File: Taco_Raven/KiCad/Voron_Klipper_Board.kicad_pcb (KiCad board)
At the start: 4 copper layers, 120 x 113 mm, 360 parts, among them J1 CONN_02X05, J10 CONN_01X04, J11 CONN_01X04, J12 CONN_02X03, J13 CONN_01X02, J14 CONN_01X02, J15 CONN_01X02, J16 CONN_01X02, J17 CONN_01X02, J18 CONN_01X02, J19 CONN_01X02, J2 CONN_02X05, J20 CONN_01X02, J21 CONN_01X02, J22 CONN_01X02, J23 CONN_01X02, J24 CONN_01X02, J25 CONN_01X06, J26 CONN_01X02, J27 CONN_01X02, J28 CONN_01X02, J29 CONN_01X03, J3 CONN_01X04, J30 CONN_01X03, J31 CONN_01X03, J32 CONN_01X03, J33 CONN_01X03, J34 USB_MINI, J35 CONN_02X05, J36 CONN_02X04, J4 CONN_01X04, J5 CONN_01X04, J6 CONN_01X04, J7 CONN_01X04, J8 CONN_01X04, J9 CONN_01X04, SW1 SW_Push, U1 TMC2130, U10 PMV40UN, U11 PMV40UN, U12 PMV40UN, U13 PMV40UN, U14 CSD18532, U15 CSD18532, U16 CSD18532, U17 CSD18532, U18 AP2112-3.3, U19 A4403, U2 TMC2130, U20 A4403, U21 ATSAMD51, U22 SPIFLASH_SOIC8, U23 PMV40UN, U3 TMC2130, U4 TMC2130, U5 TMC2130, U6 TMC2130, U7 TMC2130, U8 TMC2130, U9 PMV40UN

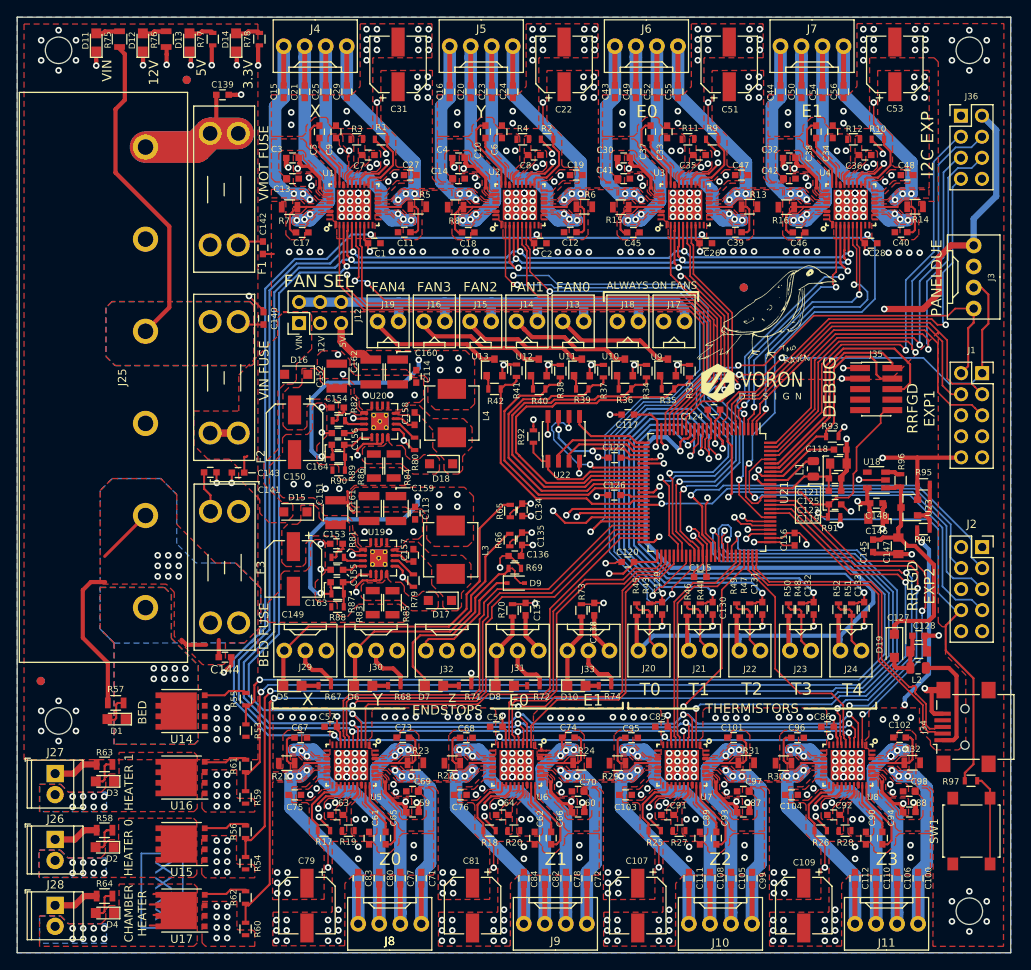
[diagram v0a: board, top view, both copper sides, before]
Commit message: Update Schematic and PCB with RevB changes
Changelog:
Footprints for J1, J2 have been mirrored.
4.7K pullups for EXP_I2C_SDA,SCL have been added.
Current sense resistors for the TMC drivers have ben lowered from 0.22Ohm to 0.11ohm to allow for more current.
Fan headers have been mirrored from Duet.
Thermistor circuits have been fixed.
R81 changed to 200k.
C163, C164 Feedforward capacitors reduced to 8.2nF and 10nF respectively.
R89 dropped to 3.48k,
R83,R84, R85,R86 Current sense kelvin connection has been improved.
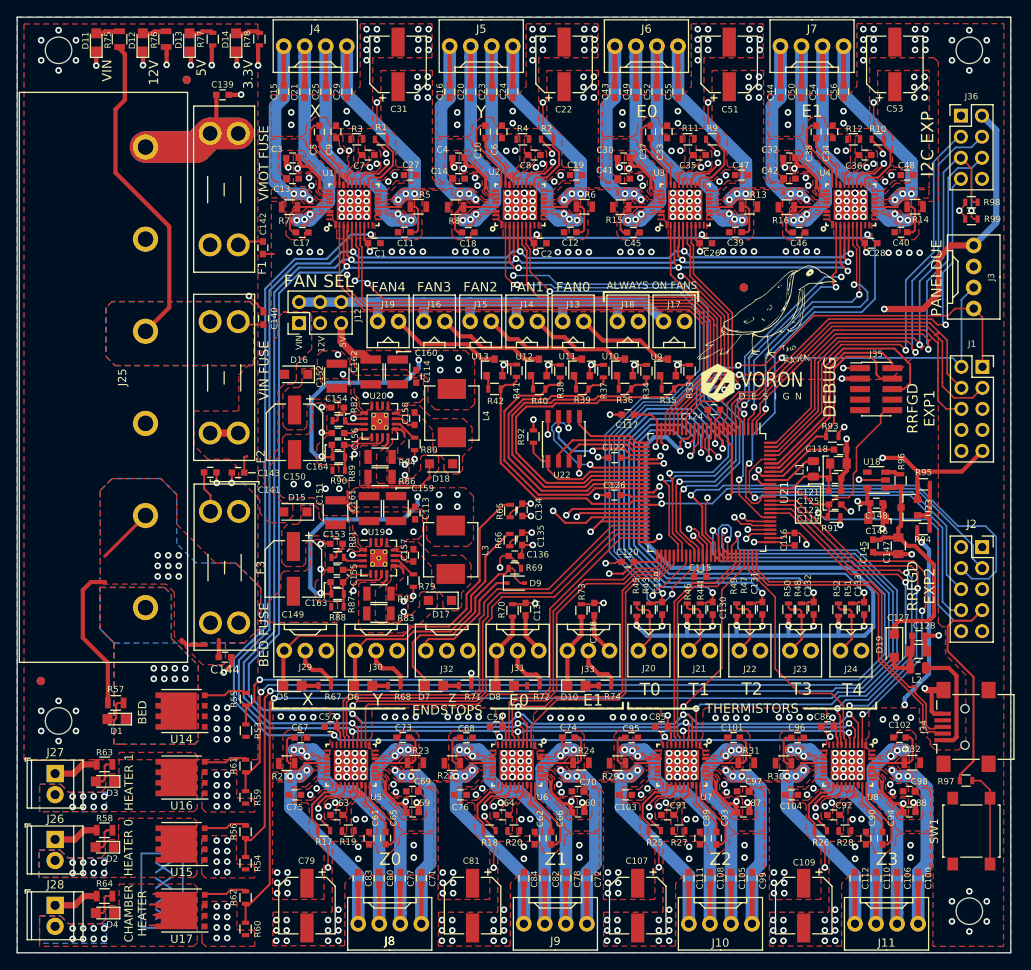
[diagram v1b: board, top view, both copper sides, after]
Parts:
- added R98: 4.70K, MZBOT:R_0603, F.Cu at (225.3, 62.4)
- added R99: 4.70K, MZBOT:R_0603, F.Cu at (225.3, 64.4)
- C163: value 100nF -> 8.2nF
- C164: value 100nF -> 10nF
- R13, R14, R15, R16, R21, R22, R23, R24, R29, R30, R31, R32, R5, R6, R7, R8: value 0R22 -> 0R11
- R43, R44, R47, R48, R51: value 10.0K -> 1.00K
- R81: value 100K -> 200K
- R89: value 3.60K -> 3.48K
- moved R85 1.97 mm to (153.7, 109.6), turned to 0 degrees
- moved R84 1.97 mm to (153.8, 93.1), turned to 0 degrees
- moved R83 1.50 mm to (153.7, 112.0), turned to 0 degrees
- moved R86 1.49 mm to (153.8, 95.5), turned to 0 degrees
- moved J1 0.77 mm to (226.6, 82.2)
- moved R97 0.60 mm to (224.6, 132.2)
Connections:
- J1 pad 1: PD_RX_RRFGD_BUZ -> PD_TX_RRFGD_BTN_ENC
- J1 pad 10: +5V -> GND
- J1 pad 2: PD_TX_RRFGD_BTN_ENC -> PD_RX_RRFGD_BUZ
- J1 pad 3: RRFGD_LCDE -> RRFGD_LCDRS
- J1 pad 4: RRFGD_LCDRS -> RRFGD_LCDE
- J1 pad 5: RRFGD_LCD4 -> (no net)
- J1 pad 6: (no net) -> RRFGD_LCD4
- J1 pad 9: GND -> +5V
- J13 pad 1: +V_FAN -> Net-(J13-Pad1)
- J13 pad 2: Net-(J13-Pad2) -> +V_FAN
- J14 pad 1: +V_FAN -> Net-(J14-Pad1)
- J14 pad 2: Net-(J14-Pad2) -> +V_FAN
- J15 pad 1: +V_FAN -> Net-(J15-Pad1)
- J15 pad 2: Net-(J15-Pad2) -> +V_FAN
- J16 pad 1: +V_FAN -> Net-(J16-Pad1)
- J16 pad 2: Net-(J16-Pad2) -> +V_FAN
- J17 pad 1: +V_FAN -> GND
- J17 pad 2: GND -> +V_FAN
- J18 pad 1: +V_FAN -> GND
- J18 pad 2: GND -> +V_FAN
- J19 pad 1: +V_FAN -> Net-(J19-Pad1)
- J19 pad 2: Net-(J19-Pad2) -> +V_FAN
- J2 pad 1: SPI_SDI -> SPI_CLK
- J2 pad 10: (no net) -> GND
- J2 pad 2: SPI_CLK -> SPI_SDI
- J2 pad 3: RRFGD_BTN_EN1 -> RRFGD_SDCSEL
- J2 pad 4: RRFGD_SDCSEL -> RRFGD_BTN_EN1
- J2 pad 5: RRFGD_BTN_EN2 -> SPI_SDO
- J2 pad 6: SPI_SDO -> RRFGD_BTN_EN2
- J2 pad 7: RRFGD_SDDET -> RESETN
- J2 pad 8: RESETN -> RRFGD_SDDET
- J2 pad 9: GND -> (no net)
- J20 pad 1: VREF -> Net-(J20-Pad1)
- J20 pad 2: Net-(J20-Pad2) -> GND
- J21 pad 1: VREF -> Net-(J21-Pad1)
- J21 pad 2: Net-(J21-Pad2) -> GND
- J22 pad 1: VREF -> Net-(J22-Pad1)
- J22 pad 2: Net-(J22-Pad2) -> GND
- J23 pad 1: VREF -> Net-(J23-Pad1)
- J23 pad 2: Net-(J23-Pad2) -> GND
- J24 pad 1: VREF -> Net-(J24-Pad1)
- J24 pad 2: Net-(J24-Pad2) -> GND
- R43 pad 1: Net-(J20-Pad2) -> Net-(J20-Pad1)
- R44 pad 1: Net-(J21-Pad2) -> Net-(J21-Pad1)
- R45 pad 2: Net-(J20-Pad2) -> Net-(J20-Pad1)
- R46 pad 2: Net-(J21-Pad2) -> Net-(J21-Pad1)
- R47 pad 1: Net-(J22-Pad2) -> Net-(J22-Pad1)
- R48 pad 1: Net-(J23-Pad2) -> Net-(J23-Pad1)
- R49 pad 2: Net-(J22-Pad2) -> Net-(J22-Pad1)
- R50 pad 2: Net-(J23-Pad2) -> Net-(J23-Pad1)
- R51 pad 1: Net-(J24-Pad2) -> Net-(J24-Pad1)
- R52 pad 2: Net-(J24-Pad2) -> Net-(J24-Pad1)
- U10 pad 3: Net-(J14-Pad2) -> Net-(J14-Pad1)
- U11 pad 3: Net-(J15-Pad2) -> Net-(J15-Pad1)
- U12 pad 3: Net-(J16-Pad2) -> Net-(J16-Pad1)
- U13 pad 3: Net-(J19-Pad2) -> Net-(J19-Pad1)
- U9 pad 3: Net-(J13-Pad2) -> Net-(J13-Pad1)
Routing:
- net Net-(J19-Pad2): track 16.2 -> 0.00 mm
- net VREF: track 111.2 -> 95.0 mm, vias 1 -> 6
- net Net-(J16-Pad2): track 16.1 -> 0.00 mm
- net Net-(J15-Pad2): track 15.6 -> 0.00 mm
- net Net-(J14-Pad2): track 15.0 -> 0.00 mm
- net Net-(J13-Pad2): track 14.6 -> 0.00 mm
- net Net-(J19-Pad1): track 0.00 -> 13.5 mm
- net Net-(J16-Pad1): track 0.00 -> 13.2 mm
- net Net-(J15-Pad1): track 0.00 -> 12.8 mm
- net Net-(D18-Pad2): track 0.00 -> 12.5 mm
- net Net-(J14-Pad1): track 0.00 -> 12.5 mm
- net +3.3V: track 484.5 -> 496.9 mm, vias 32 -> 33
- net Net-(J13-Pad1): track 0.00 -> 12.1 mm
- net RRFGD_BTN_EN1: track 49.4 -> 57.5 mm
- net Net-(J24-Pad1): track 0.00 -> 7.56 mm
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
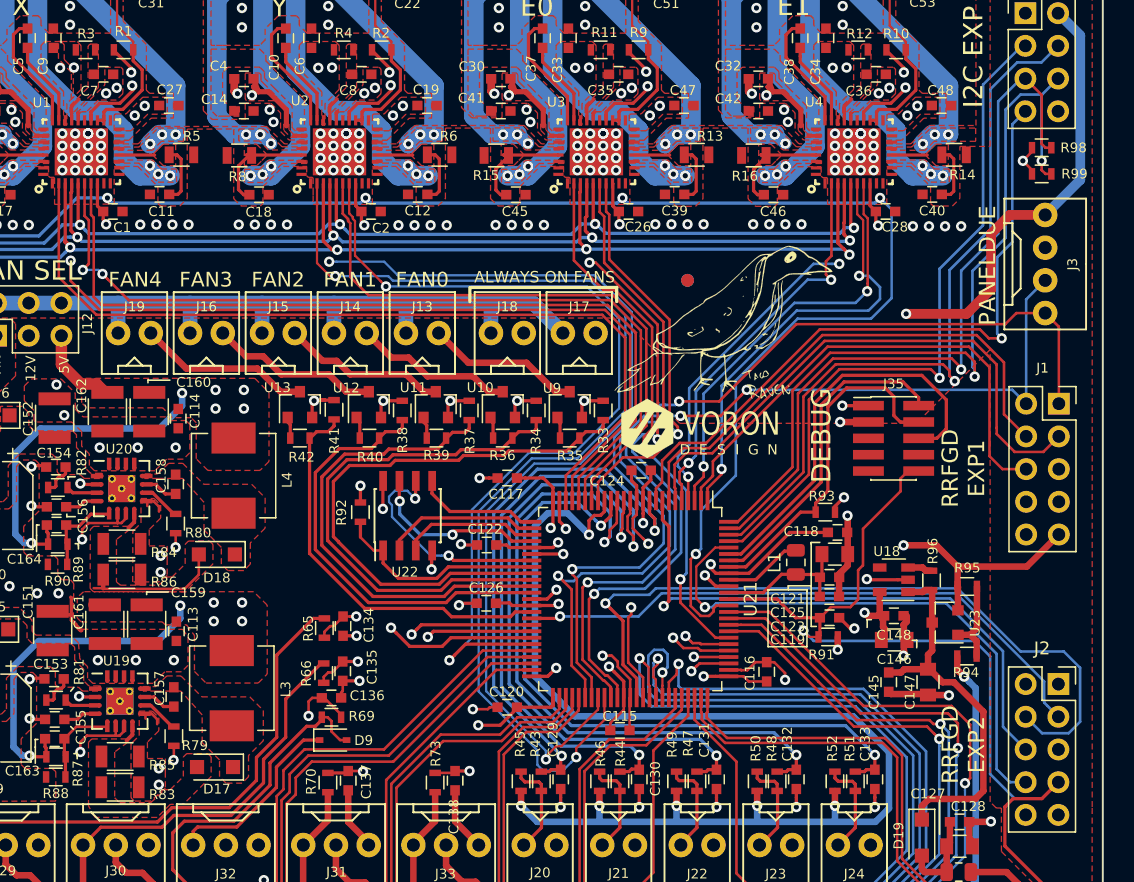
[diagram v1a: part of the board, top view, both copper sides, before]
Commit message: Gerber, Images and Assembly files updated
Updates:
     Render image
     PDF's for board and schematic
     Updated 3D models for footprints
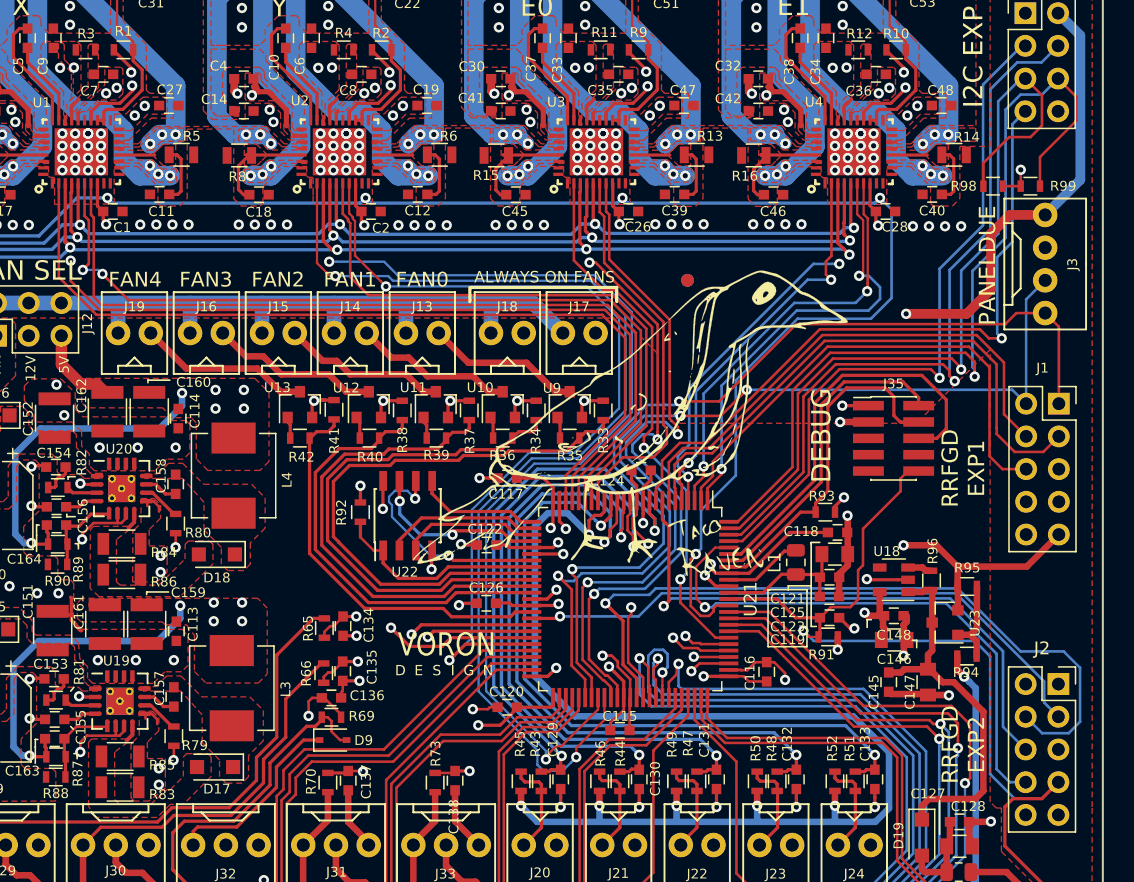
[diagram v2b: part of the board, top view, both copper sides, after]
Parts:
- removed G1: TACo, MZBOT:taco
- removed the G2 at (225.9, 133.9)
- moved R98 4.81 mm to (221.5, 65.3), turned to 180 degrees
- moved R99 1.29 mm to (224.4, 65.3)
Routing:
- net Net-(D18-Pad2): track 12.5 -> 1.26 mm
- net EXP_I2C_SDA: track 58.7 -> 64.0 mm
- net EXP_I2C_SCL: track 63.2 -> 66.5 mm, vias 2 -> 1
- net +3.3V: track 496.9 -> 498.1 mm
